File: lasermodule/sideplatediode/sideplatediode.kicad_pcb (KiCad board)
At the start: 2 copper layers, 117 x 25.2 mm, 4 parts, among them J1 Conn_01x02

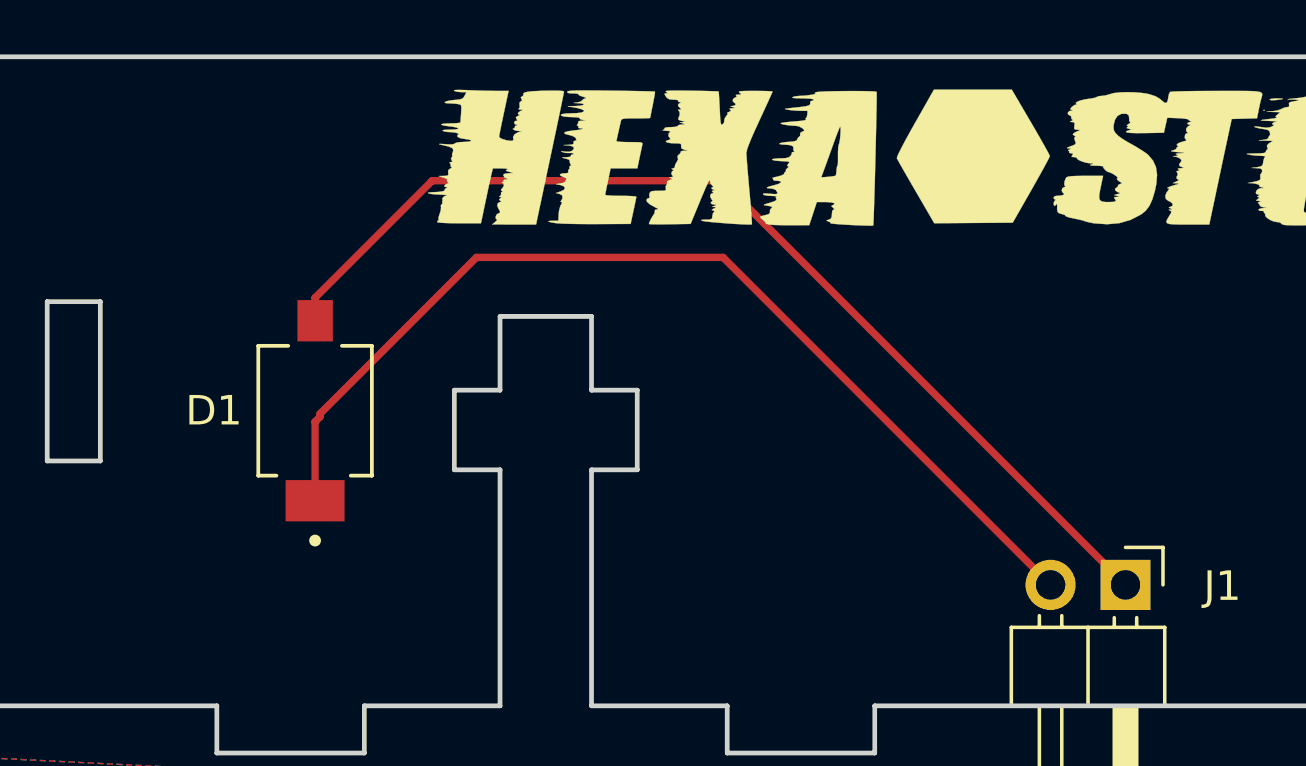
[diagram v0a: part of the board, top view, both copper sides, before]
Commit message: simplified loading in freecad, updated pcbs
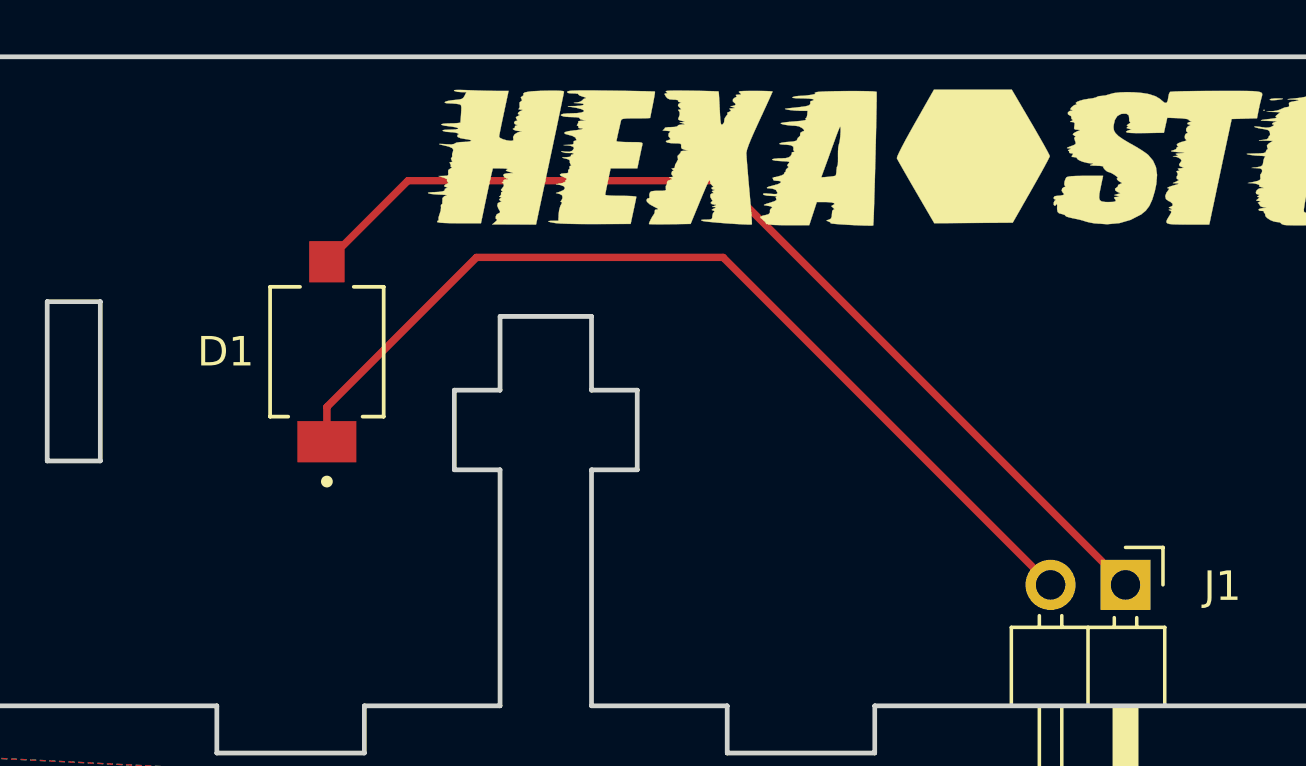
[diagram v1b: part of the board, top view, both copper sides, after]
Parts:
- moved D1 2.04 mm to (15.6, 69.4)
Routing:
- net Net-(J1-Pin_2): track 34.6 -> 32.4 mm
- net Net-(J1-Pin_1): track 35.6 -> 33.9 mm
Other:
- board text added: "PCB3D_BR_sideplatediode"
- board text added: "PCB3D_TL_sideplatediode"
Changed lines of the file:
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@@
   (net 2 "Net-(J1-Pin_2)")
   (footprint "start-of-scanline-detector:DIO_BPW_34_S-Z" (layer "F.Cu")
-    (at 15.16 71.3555 -90)
+    (at 15.56 69.3555 -90)
     (property "MANUFACTURER" "OSRAM")
     (property "PARTREV" "1.5")
@@
   (gr_line (start 19.88 70.658) (end 21.43 70.658)
     (stroke (width 0.16) (type solid)) (layer "Edge.Cuts"))
-  (segment (start 15.16 68.3055) (end 15.16 67.528) (width 0.25) (layer "F.Cu") (net 1))
-  (segment (start 15.16 67.528) (end 19.13 63.558) (width 0.25) (layer "F.Cu") (net 1))
-  (segment (start 33.98 68.608) (end 42.63 77.258) (width 0.25) (layer "F.Cu") (net 1))
-  (segment (start 19.13 63.558) (end 28.93 63.558) (width 0.25) (layer "F.Cu") (net 1))
-  (segment (start 28.93 63.558) (end 33.98 68.608) (width 0.25) (layer "F.Cu") (net 1))
+  (gr_text "PCB3D_TL_sideplatediode" (at 3.81 55.118) (layer "Cmts.User")
+    (effects (font (size 1.5 1.5) (thickness 0.3) bold) (justify left bottom))
+  )
+  (gr_text "PCB3D_BR_sideplatediode" (at 92.71 90.678) (layer "Cmts.User")
+    (effects (font (size 1.5 1.5) (thickness 0.3) bold) (justify left bottom))
+  )
+  (segment (start 18.3075 63.558) (end 28.93 63.558) (width 0.25) (layer "F.Cu") (net 1))
+  (segment (start 28.93 63.558) (end 42.63 77.258) (width 0.25) (layer "F.Cu") (net 1))
+  (segment (start 15.56 66.3055) (end 18.3075 63.558) (width 0.25) (layer "F.Cu") (net 1))
   (segment (start 28.99 66.158) (end 40.09 77.258) (width 0.25) (layer "F.Cu") (net 2))
-  (segment (start 15.33 71.558) (end 15.33 71.458) (width 0.25) (layer "F.Cu") (net 2))
-  (segment (start 15.16 74.4055) (end 15.16 71.728) (width 0.25) (layer "F.Cu") (net 2))
-  (segment (start 15.16 71.728) (end 15.33 71.558) (width 0.25) (layer "F.Cu") (net 2))
-  (segment (start 15.33 71.458) (end 20.63 66.158) (width 0.25) (layer "F.Cu") (net 2))
+  (segment (start 15.56 71.228) (end 15.56 72.4055) (width 0.25) (layer "F.Cu") (net 2))
+  (segment (start 20.63 66.158) (end 15.56 71.228) (width 0.25) (layer "F.Cu") (net 2))
   (segment (start 20.63 66.158) (end 28.99 66.158) (width 0.25) (layer "F.Cu") (net 2))
   (zone (net 1) (net_name "Net-(J1-Pin_1)") (layers "F&B.Cu") (hatch edge 0.508)

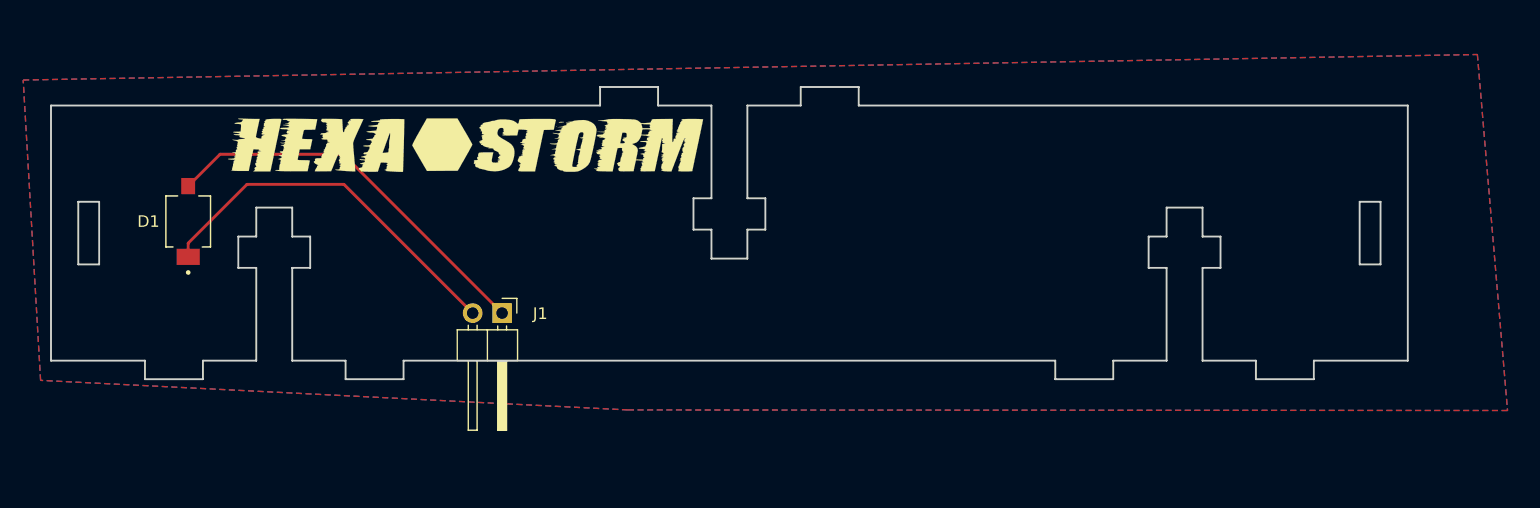
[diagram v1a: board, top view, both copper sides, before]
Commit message: pcbs can be rendered
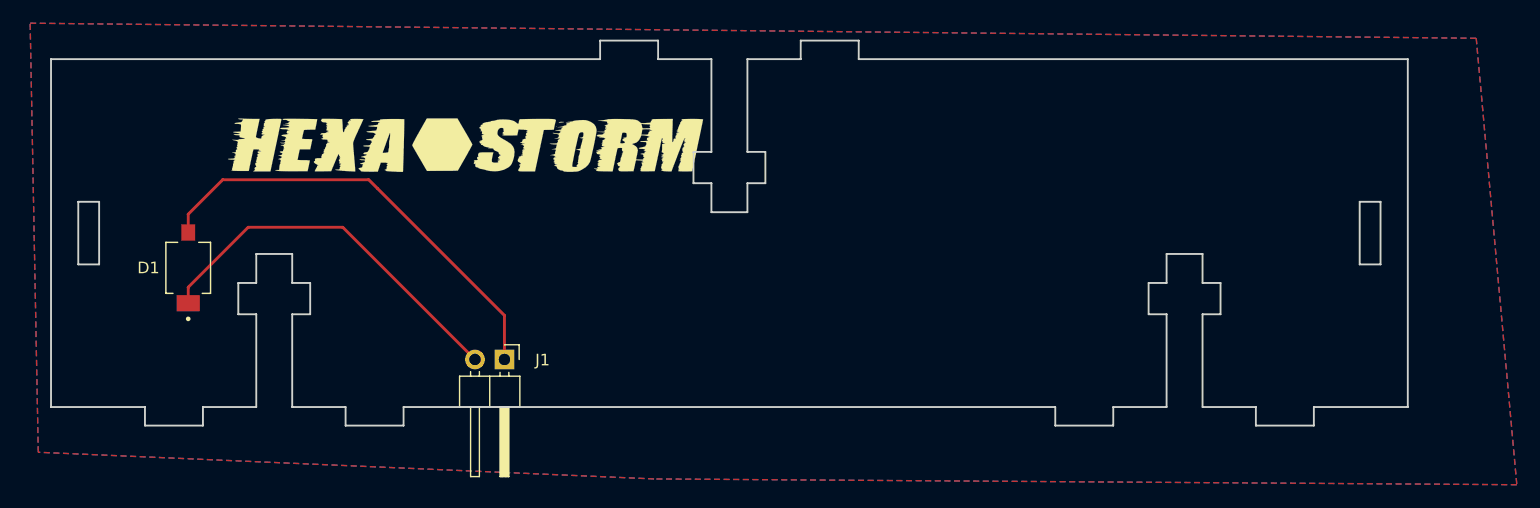
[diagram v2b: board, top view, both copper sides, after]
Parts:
- moved J1 4.00 mm to (42.8, 81.3)
- moved D1 4.00 mm to (15.6, 73.4)
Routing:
- net Net-(J1-Pin_1): track 33.9 -> 38.7 mm
- net Net-(J1-Pin_2): track 32.4 -> 33.0 mm
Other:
- board size 117 x 25.2 mm -> 117 x 33.2 mm

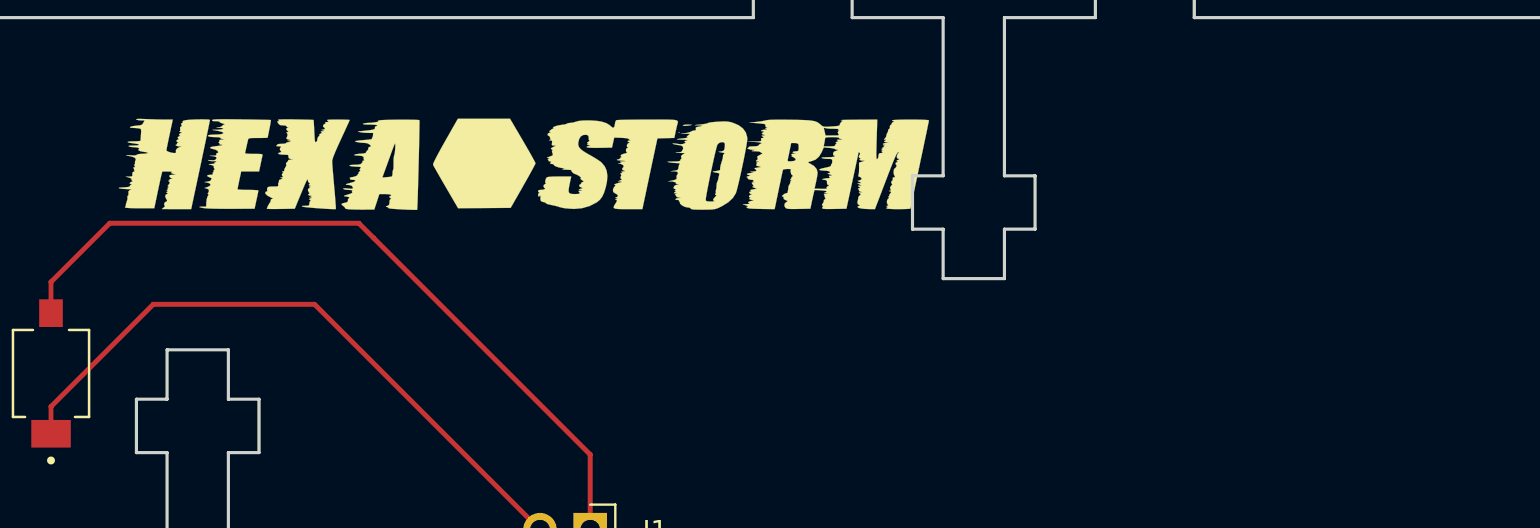
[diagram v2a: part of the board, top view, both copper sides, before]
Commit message: changed position logos
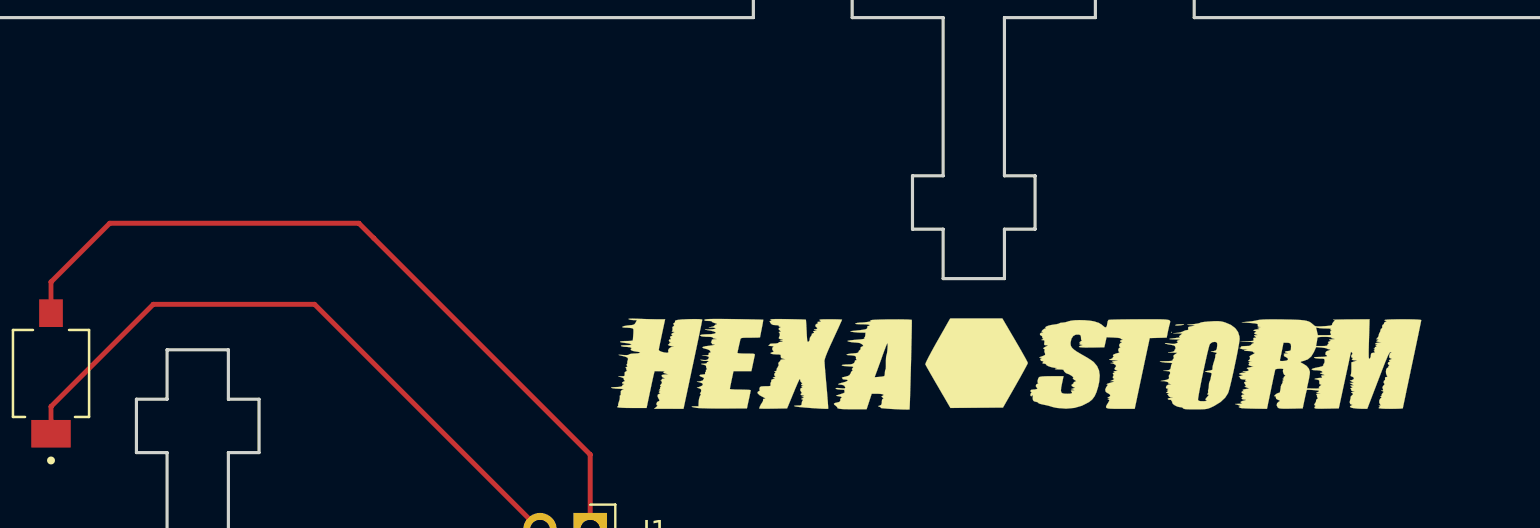
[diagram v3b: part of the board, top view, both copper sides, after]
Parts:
- moved L1 27.2 mm to (60.4, 72.9)
- moved L2 26.9 mm to (64.3, 72.9)
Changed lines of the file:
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@@
   )
   (footprint "start-of-scanline-detector:hexastorm" (layer "F.Cu")
-    (at 39.43 62.758)
+    (at 64.33 72.858)
     (property "Sheetfile" "sideplatediode.kicad_sch")
     (property "Sheetname" "")
@@
   )
   (footprint "start-of-scanline-detector:hexastorm" (layer "B.Cu")
-    (at 85.73 62.858 180)
+    (at 60.43 72.858 180)
     (property "Sheetfile" "sideplatediode.kicad_sch")
     (property "Sheetname" "")
